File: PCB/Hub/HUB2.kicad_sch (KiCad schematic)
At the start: 26 parts, among them IC1 ESP32-DEVKITC-VE, IC2 TCAN1051VDRQ1, J1 B4B-PH-SM4-TB, K1 DSY2Y-S-205H, Q2 2N2220, U1 BMP581, U10 DB301V-5.0-2P, U3 DB301V-5.0-2P, U4 DB301V-5.0-2P, U5 BMI088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

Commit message: Ouvrier_v4_test_DRC
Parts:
- added C4: 100nF, Capacitor_SMD:C_0402_1005Metric_Pad0.74x0.62mm_HandSolder, symbol Device:C
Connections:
- net +3.3V: now also C4.1
- net GNDREF: now also C4.2
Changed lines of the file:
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@@
 	)
 	(junction
+		(at 250.19 90.17)
+		(diameter 0)
+		(color 0 0 0 0)
+	)
+	(junction
 		(at 269.24 76.2)
 		(diameter 0)
@@
 	(wire
 		(pts
+			(xy 250.19 90.17) (xy 250.19 101.6)
+		)
+		(stroke
+			(width 0)
+			(type default)
+		)
+	)
+	(wire
+		(pts
 			(xy 62.23 20.32) (xy 62.23 26.67)
 		)
@@
 	(wire
 		(pts
+			(xy 243.84 91.44) (xy 243.84 90.17)
+		)
+		(stroke
+			(width 0)
+			(type default)
+		)
+	)
+	(wire
+		(pts
 			(xy 44.45 134.62) (xy 172.72 134.62)
 		)
@@
 	(wire
 		(pts
+			(xy 243.84 90.17) (xy 250.19 90.17)
+		)
+		(stroke
+			(width 0)
+			(type default)
+		)
+	)
+	(wire
+		(pts
 			(xy 124.46 71.12) (xy 129.54 71.12)
 		)
@@
 	(wire
 		(pts
+			(xy 243.84 99.06) (xy 243.84 101.6)
+		)
+		(stroke
+			(width 0)
+			(type default)
+		)
+	)
+	(wire
+		(pts
 			(xy 160.02 71.12) (xy 182.88 71.12)
 		)
@@
 	(wire
 		(pts
-			(xy 250.19 86.36) (xy 250.19 88.9)
+			(xy 250.19 86.36) (xy 250.19 90.17)
 		)
 		(stroke
@@
 	)
 	(symbol
+		(lib_id "power:GNDREF")
+		(at 243.84 101.6 0)
+		(unit 1)
+		(body_style 1)
+		(exclude_from_sim no)
+		(in_bom yes)
+		(on_board yes)
+		(in_pos_files yes)
+		(dnp no)
+		(property "Reference" "#PWR024"
+			(at 243.84 107.95 0)
+			(hide yes)
+			(show_name no)
+			(do_not_autoplace no)
+			(effects
+				(font
+					(size 1.27 1.27)
+				)
+			)
+		)
+		(property "Value" "GNDREF"
+			(at 237.998 102.616 0)
+			(show_name no)
+			(do_not_autoplace no)
+			(effects
+				(font
+					(size 1.27 1.27)
+				)
+			)
+		)
+		(property "Footprint" ""
+			(at 243.84 101.6 0)
+			(hide yes)
+			(show_name no)
+			(do_not_autoplace no)
+			(effects
+				(font
+					(size 1.27 1.27)
+				)
+			)
+		)
+		(property "Datasheet" ""
+			(at 243.84 101.6 0)
+			(hide yes)
+			(show_name no)
+			(do_not_autoplace no)
+			(effects
+				(font
+					(size 1.27 1.27)
+				)
+			)
+		)
+		(property "Description" "Power symbol creates a global label with name \"GNDREF\" , reference supply ground"
+			(at 243.84 101.6 0)
+			(hide yes)
+			(show_name no)
+			(do_not_autoplace no)
+			(effects
+				(font
+					(size 1.27 1.27)
+				)
+			)
+		)
+		(pin "1"
+		)
+		(instances
+			(project "HUB2"
+				(path "/08f5f273-7560-4bf5-9444-cae26833cf8d"
+					(reference "#PWR024")
+					(unit 1)
+				)
+			)
+		)
+	)
+	(symbol
 		(lib_id "power:+5V")
 		(at 222.25 41.91 270)
@@
 	(symbol
 		(lib_id "power:+3.3V")
-		(at 250.19 88.9 180)
+		(at 250.19 101.6 180)
 		(unit 1)
 		(body_style 1)
@@
 		(in_pos_files yes)
 		(dnp no)
-		(fields_autoplaced yes)
 		(property "Reference" "#PWR011"
-			(at 250.19 85.09 0)
+			(at 250.19 97.79 0)
 			(hide yes)
 			(show_name no)
@@
 		)
 		(property "Value" "+3.3V"
-			(at 250.19 93.98 0)
+			(at 250.19 107.95 0)
 			(show_name no)
 			(do_not_autoplace no)
@@
 		)
 		(property "Footprint" ""
-			(at 250.19 88.9 0)
+			(at 250.19 101.6 0)
 			(hide yes)
 			(show_name no)
@@
 		)
 		(property "Datasheet" ""
-			(at 250.19 88.9 0)
+			(at 250.19 101.6 0)
 			(hide yes)
 			(show_name no)
@@
 		)
 		(property "Description" "Power symbol creates a global label with name \"+3.3V\""
-			(at 250.19 88.9 0)
+			(at 250.19 101.6 0)
 			(hide yes)
 			(show_name no)
@@
 					(unit 1)
 				)
+			)
+		)
+	)
+	(symbol
+		(lib_id "Device:C")
+		(at 243.84 95.25 0)
+		(unit 1)
+		(body_style 1)
+		(exclude_from_sim no)
+		(in_bom yes)
+		(on_board yes)
+		(in_pos_files yes)
+		(dnp no)
+		(property "Reference" "C4"
+			(at 236.474 94.234 0)
+			(show_name no)
+			(do_not_autoplace no)
+			(effects
+				(font
+					(size 1.27 1.27)
+				)
+				(justify left)
+			)
+		)
+		(property "Value" "100nF"
+			(at 234.95 96.52 0)
+			(show_name no)
+			(do_not_autoplace no)
+			(effects
+				(font
+					(size 1.27 1.27)
+				)
+				(justify left)
+			)
+		)
+		(property "Footprint" "Capacitor_SMD:C_0402_1005Metric_Pad0.74x0.62mm_HandSolder"
+			(at 244.8052 99.06 0)
+			(hide yes)
+			(show_name no)
+			(do_not_autoplace no)
+			(effects
+				(font
+					(size 1.27 1.27)
+				)
+			)
+		)
+		(property "Datasheet" ""
+			(at 243.84 95.25 0)
+			(hide yes)
+			(show_name no)
+			(do_not_autoplace no)
+			(effects
+				(font
+					(size 1.27 1.27)
+				)
+			)
+		)
+		(property "Description" "Unpolarized capacitor"
+			(at 243.84 95.25 0)
+			(hide yes)
+			(show_name no)
+			(do_not_autoplace no)
+			(effects
+				(font
+					(size 1.27 1.27)
+				)
+			)
+		)
+		(pin "1"
+		)
+		(pin "2"
+		)
+		(instances
+			(project "HUB2"
+				(path "/08f5f273-7560-4bf5-9444-cae26833cf8d"
+					(reference "C4")
+					(unit 1)
+				)

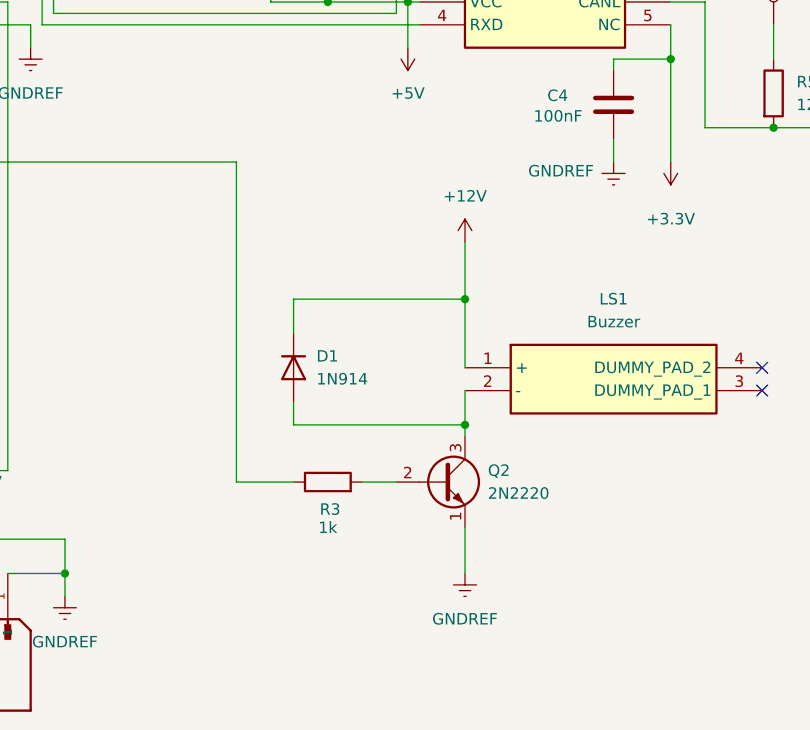
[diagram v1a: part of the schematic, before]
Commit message: changement transistor 2N2222 (empreinte)
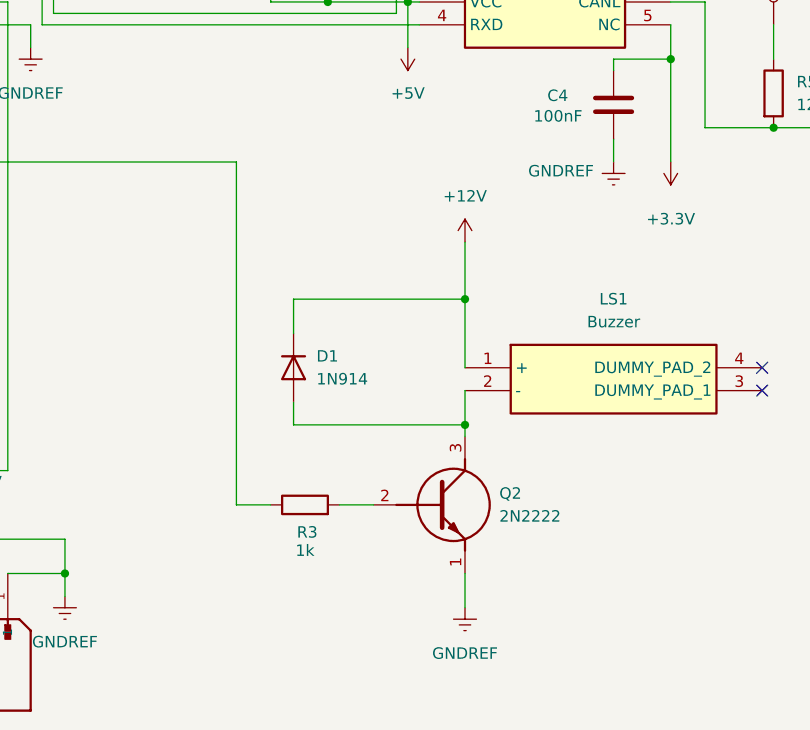
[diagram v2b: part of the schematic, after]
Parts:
- Q2: value 2N2220 -> 2N2222; footprint Package_TO_SOT_THT:TO-39-3 -> Bibliotheque_Projet:2N2222B; symbol Transistor_BJT:2N2219 -> Bibliotheque_Projet:2N2222B; Height (none) -> 7.5; Manufacturer_Name (none) -> Diotec; Manufacturer_Part_Number (none) -> 2N2222A; Mouser Part Number (none) -> 637-2N2222A; Mouser Price/Stock (none) -> https://www.mouser.co.uk/ProductDetail/Diotec-Semiconductor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
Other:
- moved on the sheet: R3
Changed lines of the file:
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@@
 	(wire
 		(pts
-			(xy 208.28 137.16) (xy 201.93 137.16)
+			(xy 205.74 139.7) (xy 201.93 139.7)
 		)
 		(stroke
@@
 	(wire
 		(pts
-			(xy 201.93 137.16) (xy 201.93 101.6)
+			(xy 201.93 139.7) (xy 201.93 101.6)
 		)
 		(stroke
@@
 	(wire
 		(pts
-			(xy 227.33 142.24) (xy 227.33 147.32)
-		)
-		(stroke
-			(width 0)
-			(type default)
-		)
-	)
-	(wire
-		(pts
 			(xy 161.29 81.28) (xy 160.02 81.28)
 		)
@@
 	(wire
 		(pts
+			(xy 227.33 147.32) (xy 227.33 151.13)
+		)
+		(stroke
+			(width 0)
+			(type default)
+		)
+	)
+	(wire
+		(pts
 			(xy 176.53 147.32) (xy 182.88 147.32)
 		)
@@
 	(wire
 		(pts
-			(xy 215.9 137.16) (xy 219.71 137.16)
+			(xy 213.36 139.7) (xy 217.17 139.7)
 		)
 		(stroke
@@
 	(symbol
 		(lib_id "power:GNDREF")
-		(at 227.33 147.32 0)
+		(at 227.33 151.13 0)
 		(unit 1)
 		(body_style 1)
@@
 		(fields_autoplaced yes)
 		(property "Reference" "#PWR014"
-			(at 227.33 153.67 0)
+			(at 227.33 157.48 0)
 			(hide yes)
 			(show_name no)
@@
 		)
 		(property "Value" "GNDREF"
-			(at 227.33 152.4 0)
+			(at 227.33 156.21 0)
 			(show_name no)
 			(do_not_autoplace no)
@@
 		)
 		(property "Footprint" ""
-			(at 227.33 147.32 0)
+			(at 227.33 151.13 0)
 			(hide yes)
 			(show_name no)
@@
 		)
 		(property "Datasheet" ""
-			(at 227.33 147.32 0)
+			(at 227.33 151.13 0)
 			(hide yes)
 			(show_name no)
@@
 		)
 		(property "Description" "Power symbol creates a global label with name \"GNDREF\" , reference supply ground"
-			(at 227.33 147.32 0)
+			(at 227.33 151.13 0)
 			(hide yes)
 			(show_name no)
@@
 	(symbol
 		(lib_id "Device:R")
-		(at 212.09 137.16 90)
+		(at 209.55 139.7 90)
 		(unit 1)
 		(body_style 1)
@@
 		(dnp no)
 		(property "Reference" "R3"
-			(at 212.344 140.208 90)
+			(at 209.804 142.748 90)
 			(show_name no)
 			(do_not_autoplace no)
@@
 		)
 		(property "Value" "1k"
-			(at 212.09 142.24 90)
+			(at 209.55 144.78 90)
 			(show_name no)
 			(do_not_autoplace no)
@@
 		)
 		(property "Footprint" "Resistor_THT:R_Axial_DIN0207_L6.3mm_D2.5mm_P10.16mm_Horizontal"
-			(at 212.09 138.938 90)
+			(at 209.55 141.478 90)
 			(hide yes)
 			(show_name no)
@@
 		)
 		(property "Datasheet" ""
-			(at 212.09 137.16 0)
+			(at 209.55 139.7 0)
 			(hide yes)
 			(show_name no)
@@
 		)
 		(property "Description" "Resistor"
-			(at 212.09 137.16 0)
+			(at 209.55 139.7 0)
 			(hide yes)
 			(show_name no)
@@
 	)
 	(symbol
-		(lib_id "Transistor_BJT:2N2219")
-		(at 224.79 137.16 0)
+		(lib_id "Bibliotheque_Projet:2N2222B")
+		(at 217.17 139.7 0)
 		(unit 1)
 		(body_style 1)
@@
 		(fields_autoplaced yes)
 		(property "Reference" "Q2"
-			(at 229.87 135.8899 0)
+			(at 231.14 138.4299 0)
 			(show_name no)
 			(do_not_autoplace no)
@@
 			)
 		)
-		(property "Value" "2N2220"
-			(at 229.87 138.4299 0)
+		(property "Value" "2N2222"
+			(at 231.14 140.9699 0)
 			(show_name no)
 			(do_not_autoplace no)
@@
 			)
 		)
-		(property "Footprint" "Package_TO_SOT_THT:TO-39-3"
-			(at 229.87 139.065 0)
+		(property "Footprint" "Bibliotheque_Projet:2N2222B"
+			(at 231.14 240.97 0)
 			(hide yes)
 			(show_name no)
@@
 				(font
 					(size 1.27 1.27)
-					(italic yes)
 				)
-				(justify left)
+				(justify left top)
 			)
 		)
-		(property "Datasheet" "http://www.onsemi.com/pub_link/Collateral/2N2219-D.PDF"
-			(at 224.79 137.16 0)
+		(property "Datasheet" "https://diotec.com/request/datasheet/2n2222a.pdf"
+			(at 231.14 340.97 0)
 			(hide yes)
 			(show_name no)
@@
 					(size 1.27 1.27)
 				)
-				(justify left)
+				(justify left top)
 			)
 		)
-		(property "Description" "800mA Ic, 50V Vce, NPN Transistor, TO-39"
-			(at 224.79 137.16 0)
+		(property "Description" "NPN General purpose transistor . IC 150 mA . f 	100 MHz"
+			(at 217.17 139.7 0)
 			(hide yes)
 			(show_name no)
@@
 		)
 		(property "Sim.Device" "NPN"
-			(at 224.79 137.16 0)
+			(at 217.17 139.7 0)
 			(hide yes)
 			(show_name no)
@@
 		)
 		(property "Sim.Pins" "1=E 2=B 3=C"
-			(at 224.79 137.16 0)
+			(at 217.17 139.7 0)
+			(hide yes)
+			(show_name no)
+			(do_not_autoplace no)
+			(effects
+				(font
+					(size 1.27 1.27)
+				)
+			)
+		)
+		(property "Height" "7.5"
+			(at 231.14 540.97 0)
+			(hide yes)
+			(show_name no)
+			(do_not_autoplace no)
+			(effects
+				(font
+					(size 1.27 1.27)
+				)
+				(justify left top)
+			)
+		)
+		(property "Mouser Part Number" "637-2N2222A"
+			(at 231.14 640.97 0)
+			(hide yes)
+			(show_name no)
+			(do_not_autoplace no)
+			(effects
+				(font
+					(size 1.27 1.27)
+				)
+				(justify left top)
+			)
+		)
+		(property "Mouser Price/Stock" "https://www.mouser.co.uk/ProductDetail/Diotec-Semiconductor/2N2222A?qs=OlC7AqGiEDmNlRSTGL2dYg%3D%3D"
+			(at 231.14 740.97 0)
 			(hide yes)
 			(show_name no)
@@
 					(size 1.27 1.27)
 				)
+				(justify left top)
+			)
+		)
+		(property "Manufacturer_Name" "Diotec"
+			(at 231.14 840.97 0)
+			(hide yes)
+			(show_name no)
+			(do_not_autoplace no)
+			(effects
+				(font
+					(size 1.27 1.27)
+				)
+				(justify left top)
+			)
+		)
+		(property "Manufacturer_Part_Number" "2N2222A"
+			(at 231.14 940.97 0)
+			(hide yes)
+			(show_name no)
+			(do_not_autoplace no)
+			(effects
+				(font
+					(size 1.27 1.27)
+				)
+				(justify left top)
 			)
 		)

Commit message: MaJ composants Hub empreinte et schematic
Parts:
- IC1: footprint projet:ESP32DEVKITCVE -> Bibliotheque_Projet:ESP32-WROVER DevKitC; symbol ESP32-DEVKITC-VE:ESP32-DEVKITC-VE -> Bibliotheque_Projet:ESP32-DEVKITC-VE
- IC2: value TCAN1051VDRQ1 -> Tranceiver_CAN; footprint projet:SOIC127P600X175-8N -> Bibliotheque_Projet:Tranceiver CAN; symbol TCAN1051VDRQ1:TCAN1051VDRQ1 -> Bibliotheque_Projet:Tranceiver_CAN
- J1: value B4B-PH-SM4-TB -> Connecteur_male_Grove_Mabee; footprint projet:CONN_JST -> Bibliotheque_Projet:Connecteur male Grove_Mabee; symbol B4B-PH-SM4-TB:B4B-PH-SM4-TB -> Bibliotheque_Projet:Connecteur_male_Grove_Mabee
- JP1: value Jumper -> Jumper CAN Hub; footprint projet:jumper -> Bibliotheque_Projet:Jumper CAN hub; symbol Jumper:Jumper_2_Bridged -> Bibliotheque_Projet:Jumper CAN Hub
- K1: footprint projet:DSY2YS205L -> Bibliotheque_Projet:Relais DSY2Y-S-205H; symbol DSY2Y-S-205L:DSY2Y-S-205L -> Bibliotheque_Projet:Relais_DSY2Y-S-205H
- LS1: value Buzzer -> Buzzer 12V; footprint projet:Sans titre -> Bibliotheque_Projet:Buzzer 12V; symbol CMT-8504-100-SMT-TR:CMT-8504-100-SMT-TR -> Bibliotheque_Projet:Buzzer_12V; now in the parts list
- U10, U3, U6, U7: value DB301V-5.0-2P -> Bornier_a_vis; footprint projet:CONN-TH_2P-P5.00_L7.6-W10.0 -> Bibliotheque_Projet:Bornier a vis; symbol Bornier:DB301V-5.0-2P -> Bibliotheque_Projet:Bornier_a_vis
- U4, U9: footprint projet:CONN-TH_2P-P5.00_L7.6-W10.0 -> Bibliotheque_Projet:Bornier a vis; symbol Bornier:DB301V-5.0-2P -> Bibliotheque_Projet:Bornier_a_vis
- U5: footprint projet:BMI088 -> Bibliotheque_Projet:BMI088; symbol Mabibliothequekicad:BMIO88 -> Bibliotheque_Projet:BMI088
- U8: footprint projet:aba -> Bibliotheque_Projet:Abaisseur tension reglable; symbol Abaisseur:Abiasseur_5V -> Bibliotheque_Projet:Abaisseur_tension_reglable
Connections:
- net GNDREF: no longer J1.SH1 (SHIELD), J1.SH2 (SHIELD)
- no-connect marks 4 -> 2
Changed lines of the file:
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@@
 	)
 	(junction
-		(at 182.88 147.32)
-		(diameter 0)
-		(color 0 0 0 0)
-	)
-	(junction
 		(at 64.77 78.74)
 		(diameter 0)
@@
 	)
 	(no_connect
-		(at 260.35 124.46)
-	)
-	(no_connect
 		(at 102.87 24.13)
 	)
-	(no_connect
-		(at 260.35 127)
-	)
 	(wire
 		(pts
@@
 	(wire
 		(pts
-			(xy 163.83 143.51) (xy 182.88 143.51)
-		)
-		(stroke
-			(width 0)
-			(type default)
-		)
-	)
-	(wire
-		(pts
 			(xy 102.87 20.32) (xy 62.23 20.32)
 		)
@@
 	(wire
 		(pts
-			(xy 182.88 143.51) (xy 182.88 147.32)
-		)
-		(stroke
-			(width 0)
-			(type default)
-		)
-	)
-	(wire
-		(pts
 			(xy 52.07 78.74) (xy 52.07 71.12)
 		)
@@
 	(wire
 		(pts
-			(xy 163.83 147.32) (xy 163.83 143.51)
-		)
-		(stroke
-			(width 0)
-			(type default)
-		)
-	)
-	(wire
-		(pts
 			(xy 269.24 76.2) (xy 274.32 76.2)
 		)
@@
 	)
 	(symbol
-		(lib_id "ESP32-DEVKITC-VE:ESP32-DEVKITC-VE")
+		(lib_id "Bibliotheque_Projet:ESP32-DEVKITC-VE")
 		(at 129.54 71.12 0)
 		(unit 1)
@@
 		(dnp no)
 		(property "Reference" "IC1"
-			(at 146.304 122.682 0)
+			(at 156.21 63.5 0)
 			(show_name no)
 			(do_not_autoplace no)
@@
 					(size 1.27 1.27)
 				)
+				(justify left top)
 			)
 		)
 		(property "Value" "ESP32-DEVKITC-VE"
-			(at 144.78 120.65 0)
+			(at 156.21 66.04 0)
 			(show_name no)
 			(do_not_autoplace no)
@@
 					(size 1.27 1.27)
 				)
+				(justify left top)
 			)
 		)
-		(property "Footprint" "projet:ESP32DEVKITCVE"
+		(property "Footprint" "Bibliotheque_Projet:ESP32-WROVER DevKitC"
 			(at 156.21 166.04 0)
 			(hide yes)
@@
 	)
 	(symbol
-		(lib_id "Bornier:DB301V-5.0-2P")
+		(lib_id "Bibliotheque_Projet:Bornier_a_vis")
 		(at 26.67 27.94 180)
 		(unit 1)
@@
 		(dnp no)
 		(property "Reference" "U3"
-			(at 19.05 30.988 0)
+			(at 21.59 29.2101 0)
 			(show_name no)
 			(do_not_autoplace no)
@@
 					(size 1.27 1.27)
 				)
+				(justify left)
 			)
 		)
-		(property "Value" "DB301V-5.0-2P"
-			(at 24.13 34.036 0)
+		(property "Value" "Bornier_a_vis"
+			(at 21.59 26.6701 0)
 			(show_name no)
 			(do_not_autoplace no)
@@
 					(size 1.27 1.27)
 				)
+				(justify left)
 			)
 		)
-		(property "Footprint" "projet:CONN-TH_2P-P5.00_L7.6-W10.0"
+		(property "Footprint" "Bibliotheque_Projet:Bornier a vis"
 			(at 26.67 19.05 0)
 			(hide yes)
@@
 	)
 	(symbol
-		(lib_id "Bornier:DB301V-5.0-2P")
+		(lib_id "Bibliotheque_Projet:Bornier_a_vis")
 		(at 26.67 19.05 180)
 		(unit 1)
@@
 			)
 		)
-		(property "Value" "DB301V-5.0-2P"
+		(property "Value" "Bornier_a_vis"
 			(at 25.4 12.7 0)
 			(show_name no)
@@
 			)
 		)
-		(property "Footprint" "projet:CONN-TH_2P-P5.00_L7.6-W10.0"
+		(property "Footprint" "Bibliotheque_Projet:Bornier a vis"
 			(at 26.67 10.16 0)
 			(hide yes)
@@
 	)
 	(symbol
-		(lib_id "CMT-8504-100-SMT-TR:CMT-8504-100-SMT-TR")
+		(lib_id "Bibliotheque_Projet:Buzzer_12V")
 		(at 227.33 124.46 0)
 		(unit 1)
 		(body_style 1)
 		(exclude_from_sim no)
-		(in_bom no)
+		(in_bom yes)
 		(on_board yes)
 		(in_pos_files yes)
@@
 		(fields_autoplaced yes)
 		(property "Reference" "LS1"
-			(at 243.84 116.84 0)
+			(at 242.57 124.4599 0)
 			(show_name no)
 			(do_not_autoplace no)
@@
 					(size 1.27 1.27)
 				)
+				(justify left)
 			)
 		)
-		(property "Value" "Buzzer"
-			(at 243.84 119.38 0)
+		(property "Value" "Buzzer 12V"
+			(at 242.57 126.9999 0)
 			(show_name no)
 			(do_not_autoplace no)
@@
 					(size 1.27 1.27)
 				)
+				(justify left)
 			)
 		)
-		(property "Footprint" "projet:Sans titre"
+		(property "Footprint" "Bibliotheque_Projet:Buzzer 12V"
 			(at 256.54 219.38 0)
 			(hide yes)
@@
 		(pin "2"
 		)
-		(pin "3"
-		)
-		(pin "4"
-		)
 		(instances
 			(project "HUB2"
@@
 	)
 	(symbol
-		(lib_id "Bornier:DB301V-5.0-2P")
+		(lib_id "Bibliotheque_Projet:Bornier_a_vis")
 		(at 278.13 67.31 0)
 		(unit 1)
@@
 			)
 		)
-		(property "Footprint" "projet:CONN-TH_2P-P5.00_L7.6-W10.0"
+		(property "Footprint" "Bibliotheque_Projet:Bornier a vis"
 			(at 278.13 76.2 0)
 			(hide yes)
@@
 	)
 	(symbol
-		(lib_id "B4B-PH-SM4-TB:B4B-PH-SM4-TB")
+		(lib_id "Bibliotheque_Projet:Connecteur_male_Grove_Mabee")
 		(at 171.45 152.4 270)
 		(unit 1)
@@
 			)
 		)
-		(property "Value" "B4B-PH-SM4-TB"
-			(at 143.256 158.242 90)
+		(property "Value" "Connecteur_male_Grove_Mabee"
+			(at 149.098 158.242 90)
 			(show_name no)
 			(do_not_autoplace no)
@@
 			)
 		)
-		(property "Footprint" "projet:CONN_JST"
+		(property "Footprint" "Bibliotheque_Projet:Connecteur male Grove_Mabee"
 			(at 171.45 152.4 0)
 			(hide yes)
@@
 		(pin "3"
 		)
-		(pin "SH2"
-		)
-		(pin "SH1"
-		)
 		(pin "1"
 		)
@@
 	)
 	(symbol
-		(lib_id "Bornier:DB301V-5.0-2P")
+		(lib_id "Bibliotheque_Projet:Bornier_a_vis")
 		(at 196.85 22.86 90)
 		(unit 1)
@@
 			)
 		)
-		(property "Value" "DB301V-5.0-2P"
+		(property "Value" "Bornier_a_vis"
 			(at 201.93 22.8599 90)
 			(show_name no)
@@
 			)
 		)
-		(property "Footprint" "projet:CONN-TH_2P-P5.00_L7.6-W10.0"
+		(property "Footprint" "Bibliotheque_Projet:Bornier a vis"
 			(at 205.74 22.86 0)
 			(hide yes)
@@
 	)
 	(symbol
-		(lib_id "Bornier:DB301V-5.0-2P")
+		(lib_id "Bibliotheque_Projet:Bornier_a_vis")
 		(at 278.13 82.55 0)
 		(unit 1)
@@
 			)
 		)
-		(property "Footprint" "projet:CONN-TH_2P-P5.00_L7.6-W10.0"
+		(property "Footprint" "Bibliotheque_Projet:Bornier a vis"
 			(at 278.13 91.44 0)
 			(hide yes)
@@
 	)
 	(symbol
-		(lib_id "Abaisseur:Abiasseur_5V")
+		(lib_id "Bibliotheque_Projet:Abaisseur_tension_reglable")
 		(at 208.28 46.99 0)
 		(unit 1)
@@
 			)
 		)
-		(property "Footprint" "projet:aba"
+		(property "Footprint" "Bibliotheque_Projet:Abaisseur tension reglable"
 			(at 208.28 46.99 0)
 			(hide yes)
@@
 	)
 	(symbol
-		(lib_id "Bornier:DB301V-5.0-2P")
+		(lib_id "Bibliotheque_Projet:Bornier_a_vis")
 		(at 189.23 22.86 90)
 		(unit 1)
@@
 		(dnp no)
 		(property "Reference" "U6"
-			(at 187.198 14.478 90)
+			(at 187.9599 17.78 0)
 			(show_name no)
 			(do_not_autoplace no)
@@
 					(size 1.27 1.27)
 				)
-				(justify right)
+				(justify left)
 			)
 		)
-		(property "Value" "DB301V-5.0-2P"
-			(at 185.928 17.272 90)
+		(property "Value" "Bornier_a_vis"
+			(at 190.4999 17.78 0)
 			(show_name no)
 			(do_not_autoplace no)
@@
 					(size 1.27 1.27)
 				)
-				(justify right)
+				(justify left)
 			)
 		)
-		(property "Footprint" "projet:CONN-TH_2P-P5.00_L7.6-W10.0"
+		(property "Footprint" "Bibliotheque_Projet:Bornier a vis"
 			(at 198.12 22.86 0)
 			(hide yes)
@@
 	)
 	(symbol
-		(lib_id "Mabibliothequekicad:BMIO88")
+		(lib_id "Bibliotheque_Projet:BMI088")
 		(at 27.94 62.23 180)
 		(unit 1)
@@
 			)
 		)
-		(property "Footprint" "projet:BMI088"
+		(property "Footprint" "Bibliotheque_Projet:BMI088"
 			(at 27.94 62.23 0)
 			(hide yes)
@@
 	)
 	(symbol
-		(lib_id "DSY2Y-S-205L:DSY2Y-S-205L")
+		(lib_id "Bibliotheque_Projet:Relais_DSY2Y-S-205H")
 		(at 67.31 24.13 0)
 		(unit 1)
@@
 			)
 		)
-		(property "Footprint" "projet:DSY2YS205L"
+		(property "Footprint" "Bibliotheque_Projet:Relais DSY2Y-S-205H"
 			(at 96.52 119.05 0)
 			(hide yes)
@@
 	)
 	(symbol
-		(lib_id "Jumper:Jumper_2_Bridged")
+		(lib_id "Bibliotheque_Projet:Jumper CAN Hub")
 		(at 261.62 81.28 270)
 		(unit 1)
@@
 			)
 		)
-		(property "Value" "Jumper"
-			(at 263.906 82.042 90)
+		(property "Value" "Jumper CAN Hub"
+			(at 254.762 81.788 90)
 			(show_name no)
 			(do_not_autoplace no)
@@
 			)
 		)
-		(property "Footprint" "projet:jumper"
+		(property "Footprint" "Bibliotheque_Projet:Jumper CAN hub"
 			(at 261.62 81.28 0)
 			(hide yes)
@@
 	)
 	(symbol
-		(lib_id "TCAN1051VDRQ1:TCAN1051VDRQ1")
+		(lib_id "Bibliotheque_Projet:Tranceiver_CAN")
 		(at 222.25 78.74 0)
 		(unit 1)
@@
 			)
 		)
-		(property "Value" "TCAN1051VDRQ1"
+		(property "Value" "Tranceiver_CAN"
 			(at 236.22 73.66 0)
 			(show_name no)
@@
 			)
 		)
-		(property "Footprint" "projet:SOIC127P600X175-8N"
+		(property "Footprint" "Bibliotheque_Projet:Tranceiver CAN"
 			(at 246.38 173.66 0)
 			(hide yes)
